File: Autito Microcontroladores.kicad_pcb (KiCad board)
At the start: 2 copper layers, 81.2 x 115.3 mm, 71 parts, among them J1 Motor izquierda, J2 Motor derecha, J3 Flash enable, J4 USB, J5 SWD, J6 BOOT MODE, J7 Batería2, J8 Bateria1, SW1 RESET, SW2 PID Init, SW3 RESET, U1 TCRT5000, U10 STM32F103C8Tx, U11 LM2596S-5, U12 AMS1117-3.3, U2 TCRT5000, U3 TCRT5000, U4 TCRT5000, U5 TCRT5000, U6 TCRT5000, U7 L9110, U8 L9110, U9 ESP-12F, Y1 8MHz

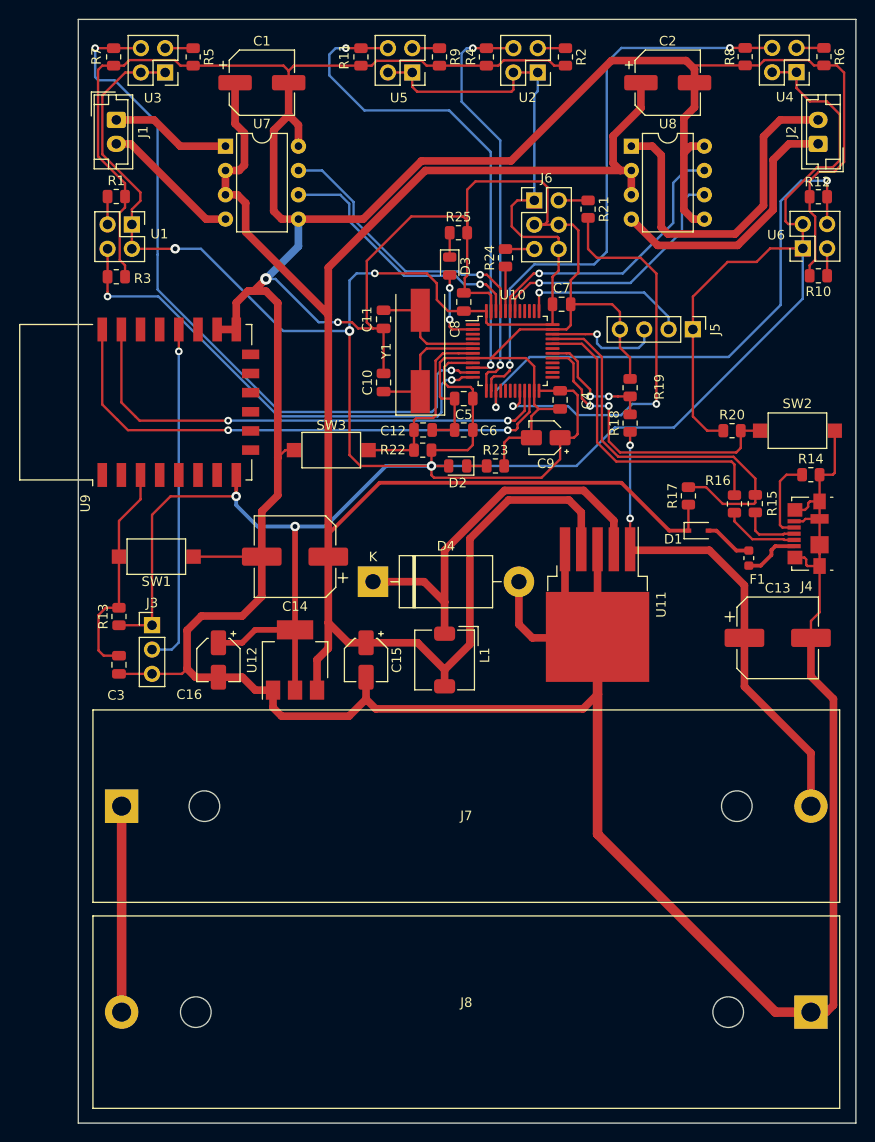
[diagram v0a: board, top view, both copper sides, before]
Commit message: Planos de tierra
Terminado el PCB con sujeciones
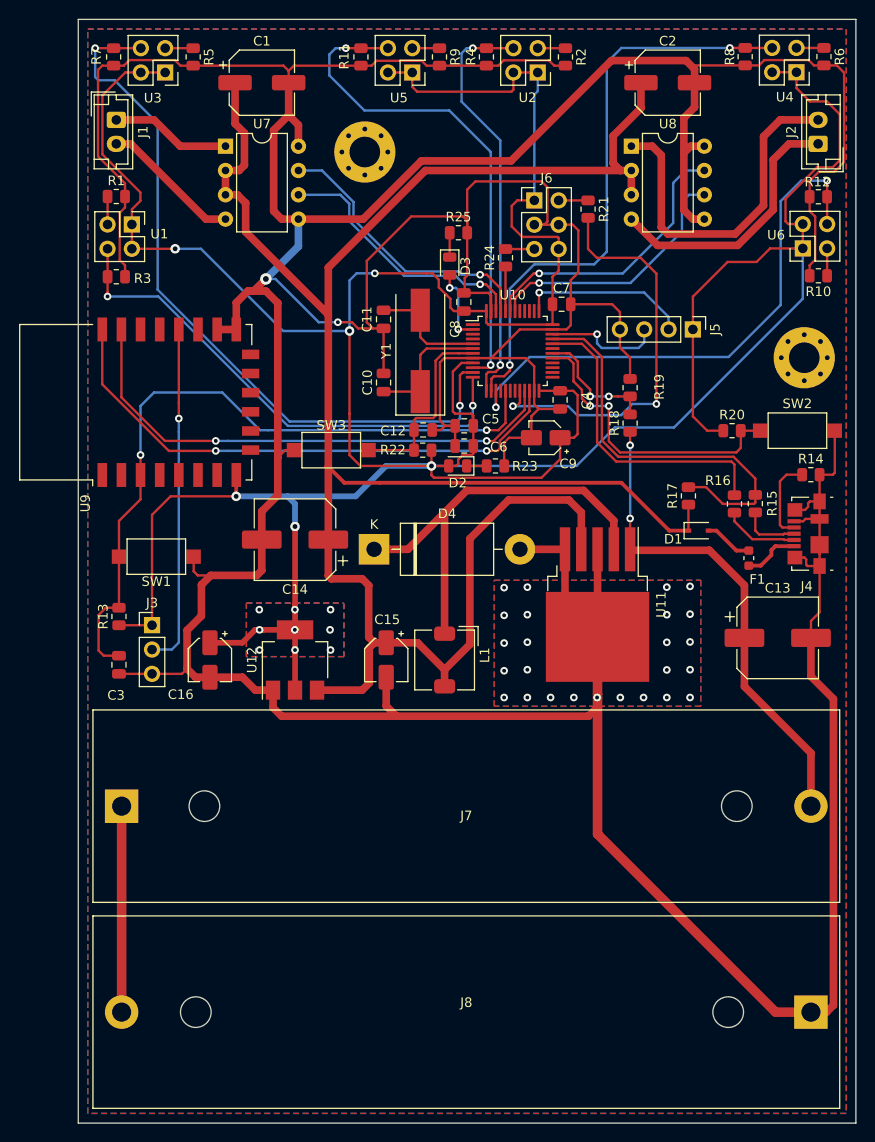
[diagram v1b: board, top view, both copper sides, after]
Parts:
- added J10: Sujeción 2, MountingHole:MountingHole_3.2mm_M3_Pad_Via, F.Cu at (140.2, 53.5)
- added J9: Sujeción 1, MountingHole:MountingHole_3.2mm_M3_Pad_Via, F.Cu at (186.1, 75.0)
- moved D4 3.39 mm to (141.1, 95.0)
- moved C5 2.85 mm to (150.6, 82.1)
- moved C15 2.11 mm to (142.4, 106.6)
- moved C14 1.78 mm to (132.9, 94.0)
- moved C6 1.68 mm to (150.6, 84.2)
- moved C16 0.89 mm to (124.0, 106.6)
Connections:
- C3 pad 1: ESP_SOFT_RESET -> ESP_SOFT_RST
- R13 pad 2: ESP_SOFT_RESET -> ESP_SOFT_RST
- SW1 pad 2: ESP_SOFT_RESET -> ESP_SOFT_RST
- U9 pad 3: ESP_SOFT_RESET -> ESP_SOFT_RST
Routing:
- net ESP_SOFT_RST: track 0.00 -> 74.5 mm, vias 0 -> 2
- net ESP_SOFT_RESET: track 23.3 -> 0.00 mm
- net GNDREF: track 641.2 -> 630.9 mm, vias 2 -> 27
- net Net-(D4-Pad1): track 41.7 -> 44.6 mm
- net SENSOR1: track 51.7 -> 53.5 mm
- net UART_TX: track 53.0 -> 54.5 mm
- net SENSOR2: track 75.8 -> 77.1 mm
- net +3V3: track 393.7 -> 392.8 mm, vias 6 -> 15
- net +5V: track 220.7 -> 219.7 mm
- net UART_RX: track 56.8 -> 57.5 mm
- added copper zone on B.Cu, net +3V3
- added copper zone on F.Cu, net +3V3
- added copper zone on B.Cu, net GNDREF
- added copper zone on F.Cu, net GNDREF

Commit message: Placa terminada
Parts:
- removed the J10 at (140.2, 53.5)
- removed the J9 at (186.1, 75.0)
- removed the U1 at (115.8, 61.1)
- removed the U2 at (158.2, 45.2)
- removed the U3 at (119.3, 45.2)
- removed the U4 at (185.3, 45.2)
- removed the U5 at (145.1, 45.2)
- removed the U6 at (185.9, 63.6)
- added +3.3V: TestPoint, TestPoint:TestPoint_Pad_D3.0mm, F.Cu at (125.7, 100.5)
- added +5V: TestPoint, TestPoint:TestPoint_Pad_D3.0mm, F.Cu at (145.7, 100.1)
- added +BATT: TestPoint, TestPoint:TestPoint_Pad_D3.0mm, F.Cu at (174.3, 78.5)
- added FID1: Fiducial, Fiducial:Fiducial_1mm_Mask2mm, F.Cu at (177.3, 109.9)
- added FID2: Fiducial, Fiducial:Fiducial_1mm_Mask2mm, F.Cu at (186.1, 59.4)
- added FID3: Fiducial, Fiducial:Fiducial_1mm_Mask2mm, F.Cu at (133.7, 74.9)
- added G***: LOGO, Mis_componentes:UNER, B.Cu at (150.8, 132.0)
- added GNDREF: TestPoint, TestPoint:TestPoint_Pad_D3.0mm, F.Cu at (125.0, 91.9)
- added H1: MountingHole, MountingHole:MountingHole_3.2mm_M3_Pad_Via, F.Cu at (185.1, 75.5)
- added H2: MountingHole, MountingHole:MountingHole_3.2mm_M3_Pad_Via, F.Cu at (123.9, 65.9)
- added J1: SENSOR 1, Mis_componentes:TCRT5000, F.Cu at (113.7, 70.5)
- added J2: SENSOR 4, Mis_componentes:TCRT5000, F.Cu at (154.4, 42.6)
- added J3: SENSOR 2, Mis_componentes:TCRT5000, F.Cu at (116.9, 43.1)
- added J4: SENSOR 5, Mis_componentes:TCRT5000, F.Cu at (177.2, 43.1)
- added J5: SENSOR 3, Mis_componentes:TCRT5000, F.Cu at (139.0, 47.1)
- added J6: SENSOR 6, Mis_componentes:TCRT5000, F.Cu at (188.0, 61.9)
- added MOTDA: TestPoint, TestPoint:TestPoint_Pad_D3.0mm, F.Cu at (179.1, 58.0)
- added MOTDB: TestPoint, TestPoint:TestPoint_Pad_D3.0mm, F.Cu at (179.1, 52.1)
- added MOTIA: TestPoint, TestPoint:TestPoint_Pad_D3.0mm, F.Cu at (140.2, 55.5)
- added MOTIB: TestPoint, TestPoint:TestPoint_Pad_D3.0mm, F.Cu at (138.0, 50.5)
- added NT1: Net-Tie_2, NetTie:NetTie-2_SMD_Pad2.0mm, F.Cu at (164.5, 112.3)
- R1, R10, R2, R5, R6, R9: value 120R -> 50k
- R11, R12, R3, R4, R7, R8: value 50k -> 120R
- moved R12 11.6 mm to (183.2, 68.9), turned to 0 degrees
- moved R1 11.3 mm to (118.5, 68.6)
- moved R7 10.9 mm to (123.9, 48.0), turned to 90 degrees
- moved R6 10.1 mm to (179.1, 48.0)
- moved R4 8.87 mm to (157.9, 50.9), turned to 90 degrees
- moved R9 8.83 mm to (143.1, 50.9)
- moved R11 8.49 mm to (146.6, 48.6), turned to 180 degrees
- moved R2 8.30 mm to (154.5, 48.6), turned to 180 degrees
- moved R8 6.13 mm to (184.2, 48.0), turned to 90 degrees
- moved R5 5.59 mm to (118.8, 48.0)
- moved R3 5.28 mm to (118.5, 63.5), turned to 180 degrees
- moved R10 5.11 mm to (183.2, 63.8)
- moved C2 2.91 mm to (168.9, 46.2)
- moved C1 2.40 mm to (131.8, 46.2)
- moved J10 1.14 mm to (187.6, 93.4)
- renumbered J4 to J10, J5 to J11, J6 to J12, J7 to J13, J8 to J14, J1 to J7, J2 to J8, J3 to J9, U7 to U1, U8 to U2, U9 to U3, U10 to U4, U11 to U5, U12 to U6
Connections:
- J12 pad 1: +3V3 -> GNDREF
- J12 pad 2: Net-(J6-Pad2) -> GNDREF
- J12 pad 3: GNDREF -> Net-(J12-Pad3)
- J12 pad 4: GNDREF -> Net-(J12-Pad4)
- J12 pad 5: Net-(J6-Pad5) -> +3V3
- R1 pad 1: Net-(R1-Pad1) -> SENSOR1
- R10 pad 1: Net-(R10-Pad1) -> SENSOR6
- R11 pad 1: SENSOR3 -> GNDREF
- R11 pad 2: GNDREF -> Net-(J5-Pad2)
- R12 pad 1: SENSOR6 -> GNDREF
- R12 pad 2: GNDREF -> Net-(J6-Pad2)
- R2 pad 1: Net-(R2-Pad1) -> SENSOR4
- R21 pad 1: Net-(J6-Pad2) -> Net-(J12-Pad3)
- R24 pad 2: Net-(J6-Pad5) -> Net-(J12-Pad4)
- R3 pad 1: SENSOR1 -> GNDREF
- R3 pad 2: GNDREF -> Net-(J1-Pad2)
- R4 pad 1: SENSOR4 -> GNDREF
- R4 pad 2: GNDREF -> Net-(J2-Pad2)
- R5 pad 1: Net-(R5-Pad1) -> SENSOR2
- R6 pad 1: Net-(R6-Pad1) -> SENSOR5
- R7 pad 1: SENSOR2 -> GNDREF
- R7 pad 2: GNDREF -> Net-(J3-Pad2)
- R8 pad 1: SENSOR5 -> GNDREF
- R8 pad 2: GNDREF -> Net-(J4-Pad2)
- R9 pad 1: Net-(R9-Pad1) -> SENSOR3
- U5 pad 3: GNDREF -> GND1
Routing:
- net GNDREF: track 630.9 -> 513.9 mm, vias 27 -> 2
- net GND1: track 0.00 -> 25.1 mm, vias 0 -> 24
- net +3V3: track 392.8 -> 406.6 mm, vias 15 -> 14
- net SENSOR6: track 58.0 -> 46.7 mm
- net +BATT: track 51.7 -> 61.4 mm
- net MOTIA: track 27.7 -> 37.0 mm
- net MOTIB: track 29.6 -> 38.6 mm
- net Net-(J12-Pad4): track 0.00 -> 7.81 mm
- net Net-(J12-Pad3): track 0.00 -> 7.32 mm
- net SENSOR5: track 61.5 -> 54.2 mm, vias 2 -> 1
- net SENSOR3: track 53.0 -> 45.8 mm, vias 2 -> 1
- net MOTDB: track 29.7 -> 36.0 mm
- net SENSOR2: track 77.1 -> 71.0 mm, vias 2 -> 1
- net +5V: track 219.7 -> 224.3 mm
- net Net-(J2-Pad2): track 0.00 -> 4.46 mm
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- added copper zone on B.Cu, net GND1
- added copper zone on F.Cu, net GND1
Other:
- board text added: "+"
- board text added: "+3.3V"
- board text added: "-"
- board text added: "BOOT0"
- board text added: "BOOT1"
- board text added: "ESP_FLASH"
- board text added: "GNDREF"
- board text added: "SWCLK"
- board text added: "SWDIO"

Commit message: Entrega de PCB
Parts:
- added G***: LOGO, Mis_componentes:Nombre_materia, B.Cu at (151.0, 148.0)

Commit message: Entrega
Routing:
- net GNDREF: track 513.9 -> 512.9 mm
